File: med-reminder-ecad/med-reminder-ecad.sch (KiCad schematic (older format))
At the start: 38 parts, among them J1 USB_B_Micro, J2 22-03-5035, J3 22-03-5025, J4 22-03-5065, Q1 2N3904, Q2 2N3904, Q3 2N3904, Q4 2N3904, SW1 SW_SPDT, SW2 SW_Push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

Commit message: Changed OSC footprint size, changed switch footprint.
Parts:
- SW1: footprint Button_Switch_THT:SW_PUSH_6mm -> Button_Switch_THT:SW_Push_1P2T_Vertical_E-Switch_800UDP8P1A1M6
- Y1: footprint Oscillator:Oscillator_DIP-14 -> Oscillator:Oscillator_DIP-8; Mfg PN (none) -> MXO45HS-3C-8M0000
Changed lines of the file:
@@
 F 0 "SW1" H 1000 6835 50  0000 C CNN
 F 1 "SW_SPDT" H 1000 6744 50  0000 C CNN
-F 2 "Button_Switch_THT:SW_PUSH_6mm" H 1000 6550 50  0001 C CNN
+F 2 "Button_Switch_THT:SW_Push_1P2T_Vertical_E-Switch_800UDP8P1A1M6" H 1000 6550 50  0001 C CNN
 F 3 "~" H 1000 6550 50  0001 C CNN
 F 4 "1" H 1000 6550 50  0001 C CNN "DNP"
@@
 F 0 "Y1" H 6600 3268 50  0000 C CNN
 F 1 "8MHz" H 6600 3177 50  0000 C CNN
-F 2 "Oscillator:Oscillator_DIP-14" H 6600 3000 50  0001 C CNN
+F 2 "Oscillator:Oscillator_DIP-8" H 6600 3000 50  0001 C CNN
 F 3 "~" H 6600 3000 50  0001 C CNN
 F 4 "1" H 6600 3000 50  0001 C CNN "DNP"
+F 5 "MXO45HS-3C-8M0000" H 6600 3000 50  0001 C CNN "Mfg PN"
 	1    6600 3000
 	1    0    0    -1

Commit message: WIP update for PCB layout
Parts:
- C6: footprint Capacitor_THT:C_Rect_L7.0mm_W4.5mm_P5.00mm -> Capacitor_Tantalum_SMD:CP_EIA-3216-10_Kemet-I
- Y1: footprint Oscillator:Oscillator_DIP-8 -> Crystal:Crystal_HC33-U_Vertical
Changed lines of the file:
@@
 F 0 "C6" H 9092 1546 50  0000 L CNN
 F 1 "100nF" H 9092 1455 50  0000 L CNN
-F 2 "Capacitor_THT:C_Rect_L7.0mm_W4.5mm_P5.00mm" H 9000 1500 50  0001 C CNN
+F 2 "Capacitor_Tantalum_SMD:CP_EIA-3216-10_Kemet-I" H 9000 1500 50  0001 C CNN
 F 3 "~" H 9000 1500 50  0001 C CNN
 	1    9000 1500
@@
 F 0 "Y1" H 6600 3268 50  0000 C CNN
 F 1 "8MHz" H 6600 3177 50  0000 C CNN
-F 2 "Oscillator:Oscillator_DIP-8" H 6600 3000 50  0001 C CNN
+F 2 "Crystal:Crystal_HC33-U_Vertical" H 6600 3000 50  0001 C CNN
 F 3 "~" H 6600 3000 50  0001 C CNN
 F 4 "1" H 6600 3000 50  0001 C CNN "DNP"

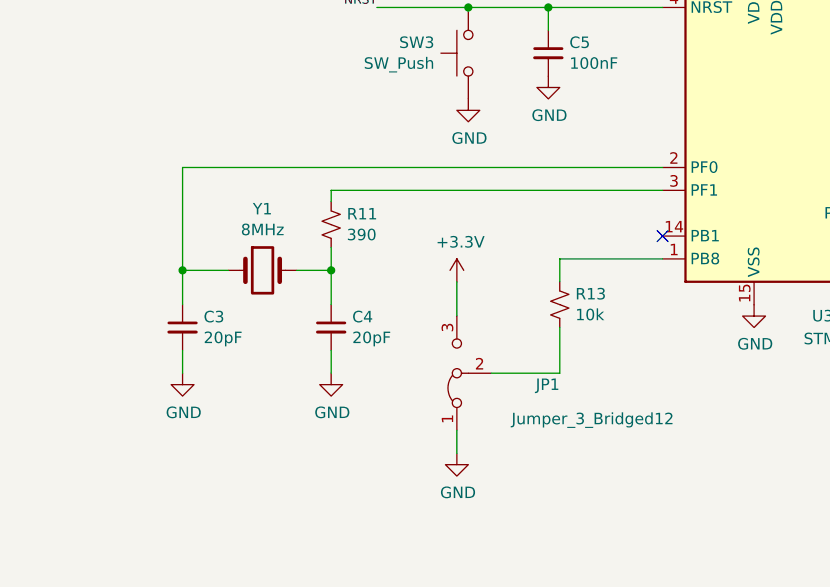
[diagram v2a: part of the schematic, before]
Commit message: Removed oscillator circuit
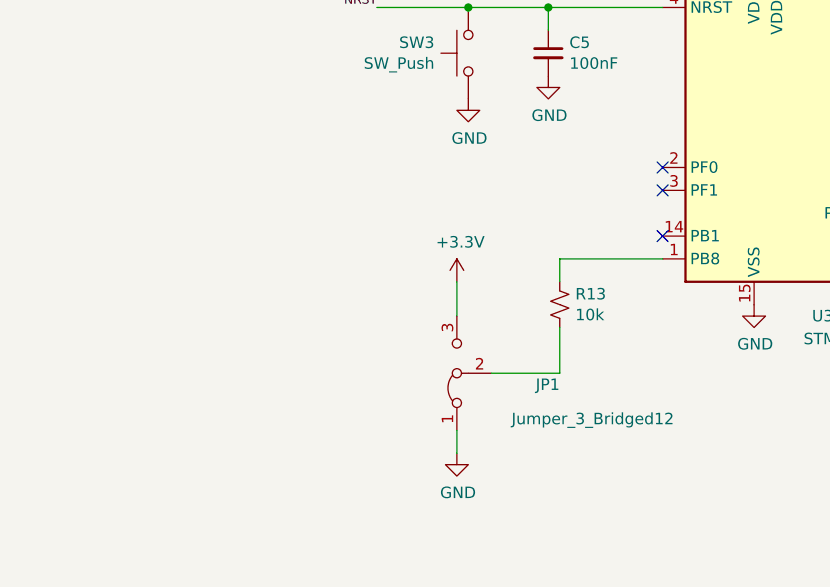
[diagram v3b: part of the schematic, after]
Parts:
- removed C3, C4: 20pF, Capacitor_THT:C_Rect_L7.0mm_W4.5mm_P5.00mm, symbol Device:C_Small
- removed R11: 390, Resistor_THT:R_Axial_DIN0204_L3.6mm_D1.6mm_P5.08mm_Horizontal, symbol Device:R_Small_US
- removed Y1: 8MHz, Crystal:Crystal_HC33-U_Vertical, symbol Device:Crystal
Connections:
- no-connect marks 5 -> 7
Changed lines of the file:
@@
 Connection ~ 9500 1600
-$Comp
-L Device:Crystal Y1
-U 1 1 60581513
-P 6600 3000
-F 0 "Y1" H 6600 3268 50  0000 C CNN
-F 1 "8MHz" H 6600 3177 50  0000 C CNN
-F 2 "Crystal:Crystal_HC33-U_Vertical" H 6600 3000 50  0001 C CNN
-F 3 "~" H 6600 3000 50  0001 C CNN
-F 4 "1" H 6600 3000 50  0001 C CNN "DNP"
-F 5 "MXO45HS-3C-8M0000" H 6600 3000 50  0001 C CNN "Mfg PN"
-	1    6600 3000
-	1    0    0    -1
-$EndComp
-$Comp
-L Device:C_Small C4
-U 1 1 60582666
-P 6900 3250
-F 0 "C4" H 6992 3296 50  0000 L CNN
-F 1 "20pF" H 6992 3205 50  0000 L CNN
-F 2 "Capacitor_THT:C_Rect_L7.0mm_W4.5mm_P5.00mm" H 6900 3250 50  0001 C CNN
-F 3 "~" H 6900 3250 50  0001 C CNN
-F 4 "1" H 6900 3250 50  0001 C CNN "DNP"
-	1    6900 3250
-	1    0    0    -1
-$EndComp
-$Comp
-L Device:C_Small C3
-U 1 1 60585144
-P 6250 3250
-F 0 "C3" H 6342 3296 50  0000 L CNN
-F 1 "20pF" H 6342 3205 50  0000 L CNN
-F 2 "Capacitor_THT:C_Rect_L7.0mm_W4.5mm_P5.00mm" H 6250 3250 50  0001 C CNN
-F 3 "~" H 6250 3250 50  0001 C CNN
-F 4 "1" H 6250 3250 50  0001 C CNN "DNP"
-	1    6250 3250
-	1    0    0    -1
-$EndComp
-$Comp
-L power:GND #PWR0110
-U 1 1 60585535
-P 6900 3450
-F 0 "#PWR0110" H 6900 3200 50  0001 C CNN
-F 1 "GND" H 6905 3277 50  0000 C CNN
-F 2 "" H 6900 3450 50  0001 C CNN
-F 3 "" H 6900 3450 50  0001 C CNN
-	1    6900 3450
-	1    0    0    -1
-$EndComp
-$Comp
-L power:GND #PWR0111
-U 1 1 60586789
-P 6250 3450
-F 0 "#PWR0111" H 6250 3200 50  0001 C CNN
-F 1 "GND" H 6255 3277 50  0000 C CNN
-F 2 "" H 6250 3450 50  0001 C CNN
-F 3 "" H 6250 3450 50  0001 C CNN
-	1    6250 3450
-	1    0    0    -1
-$EndComp
-Wire Wire Line
-	6250 3350 6250 3450
-Wire Wire Line
-	6900 3450 6900 3350
-Wire Wire Line
-	6900 3150 6900 3000
-Wire Wire Line
-	6900 3000 6750 3000
-Wire Wire Line
-	6250 3150 6250 3000
-Wire Wire Line
-	6250 3000 6450 3000
-Wire Wire Line
-	6250 2550 6250 3000
-Connection ~ 6250 3000
-$Comp
-L Device:R_Small_US R11
-U 1 1 6058A97D
-P 6900 2800
-F 0 "R11" H 6968 2846 50  0000 L CNN
-F 1 "390" H 6968 2755 50  0000 L CNN
-F 2 "Resistor_THT:R_Axial_DIN0204_L3.6mm_D1.6mm_P5.08mm_Horizontal" H 6900 2800 50  0001 C CNN
-F 3 "~" H 6900 2800 50  0001 C CNN
-F 4 "1" H 6900 2800 50  0001 C CNN "DNP"
-	1    6900 2800
-	1    0    0    -1
-$EndComp
-Wire Wire Line
-	6900 2900 6900 3000
-Connection ~ 6900 3000
-Wire Wire Line
-	6250 2550 8350 2550
-Wire Wire Line
-	6900 2700 6900 2650
-Wire Wire Line
-	6900 2650 8350 2650
 $Comp
 L Jumper:Jumper_3_Bridged12 JP1
@@
 Wire Wire Line
 	1600 2150 1600 2050
+NoConn ~ 8350 2550
+NoConn ~ 8350 2650
 $EndSCHEMATC

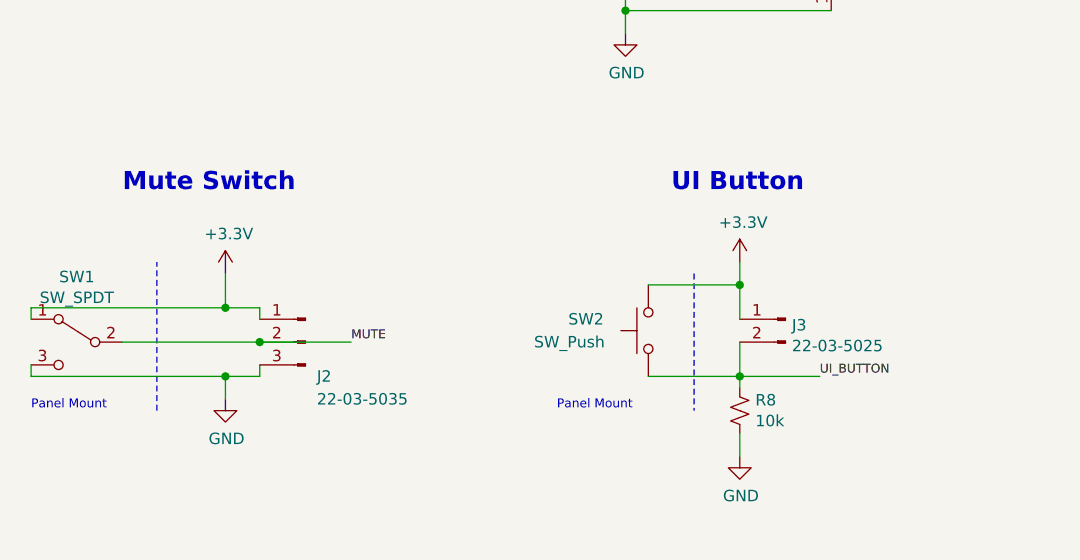
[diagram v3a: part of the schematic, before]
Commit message: Changed footprint of UI elements to be MOLEX SL connectors
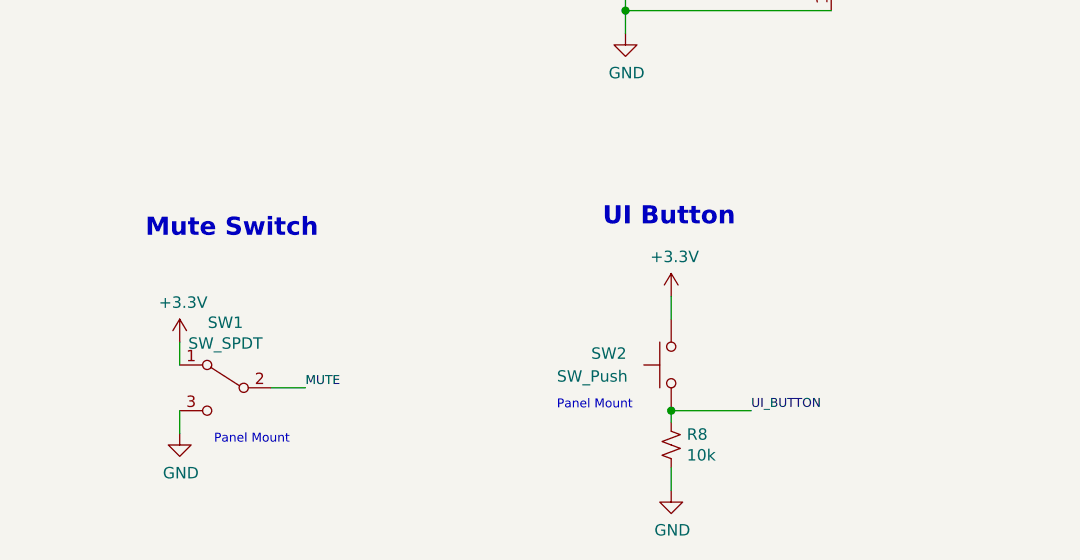
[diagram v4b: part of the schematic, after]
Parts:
- removed J2: 22-03-5035, Connector_Molex:Molex_SPOX_5267-03A_1x03_P2.50mm_Vertical, symbol Connector:Conn_01x03_Male
- removed J3: 22-03-5025, Connector_Molex:Molex_SPOX_5267-02A_1x02_P2.50mm_Vertical, symbol Connector:Conn_01x02_Male
- BZ1: footprint Connector_PinHeader_2.54mm:PinHeader_1x02_P2.54mm_Vertical -> Connector_Molex:Molex_SL_171971-0002_1x02_P2.54mm_Vertical
- SW1: footprint Button_Switch_THT:SW_Push_1P2T_Vertical_E-Switch_800UDP8P1A1M6 -> Connector_Molex:Molex_SL_171971-0003_1x03_P2.54mm_Vertical
- SW2: footprint Button_Switch_THT:SW_PUSH_6mm -> Connector_Molex:Molex_SL_171971-0002_1x02_P2.54mm_Vertical
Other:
- moved on the sheet: R8, SW1, SW2

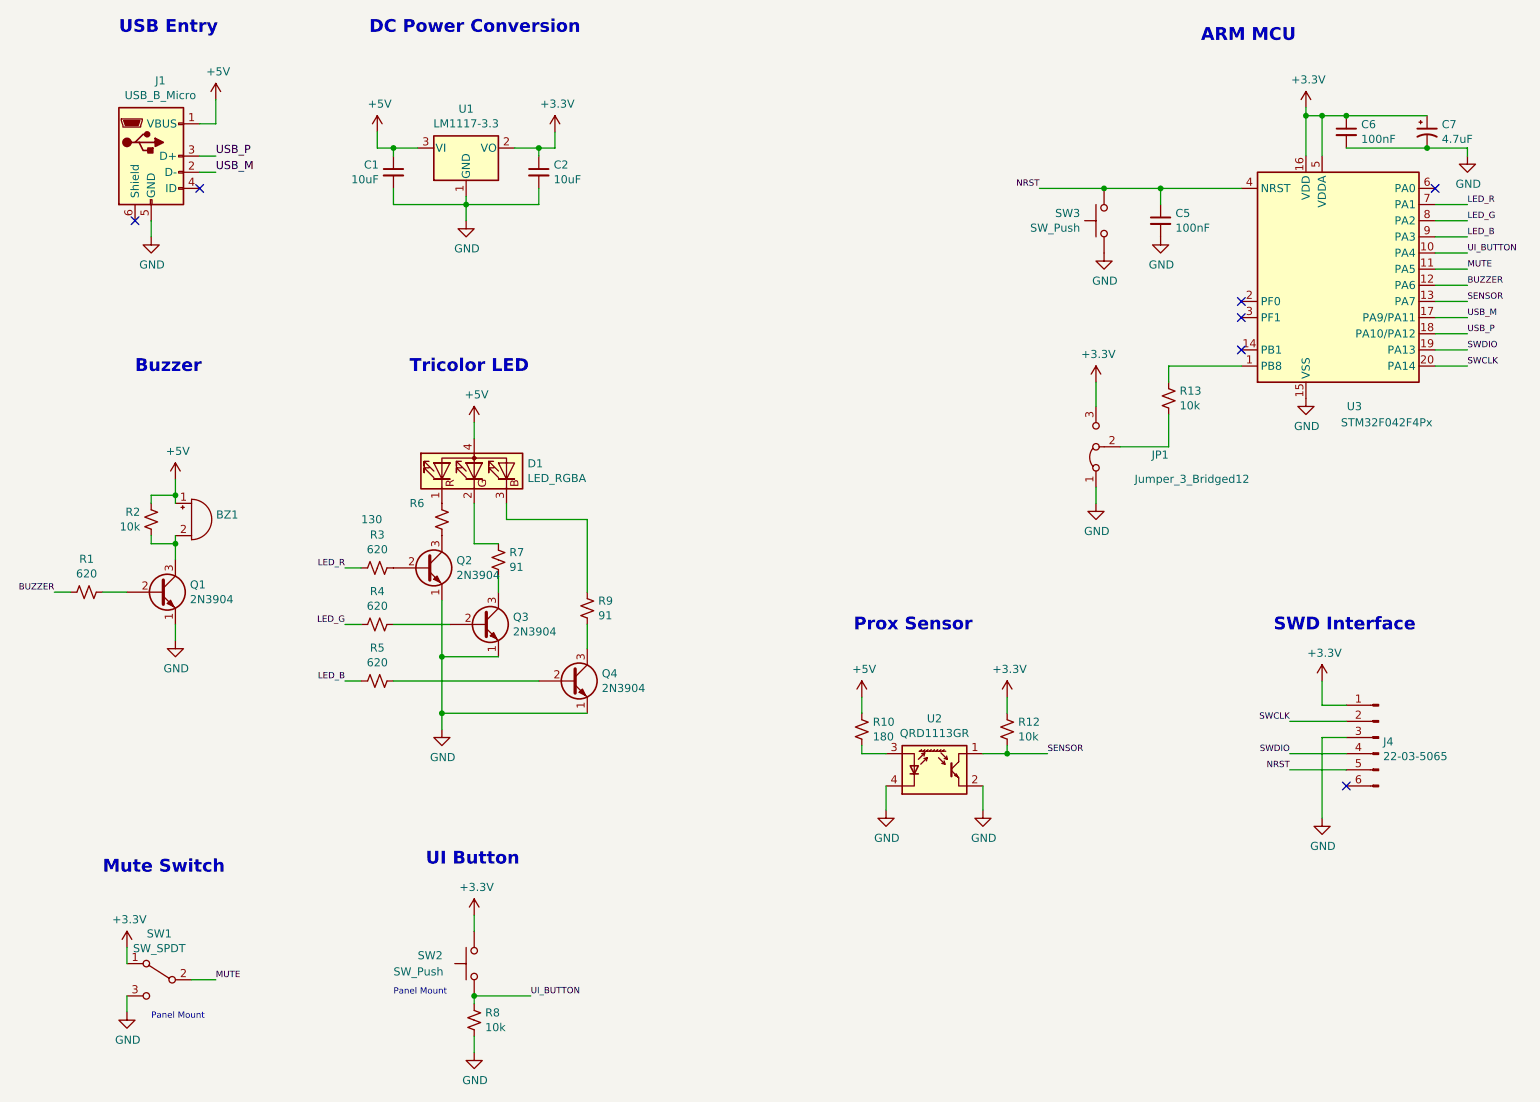
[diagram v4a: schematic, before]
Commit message: Broke out LED board to heirarchal sheet to become a separate board, replaced some components with SMD
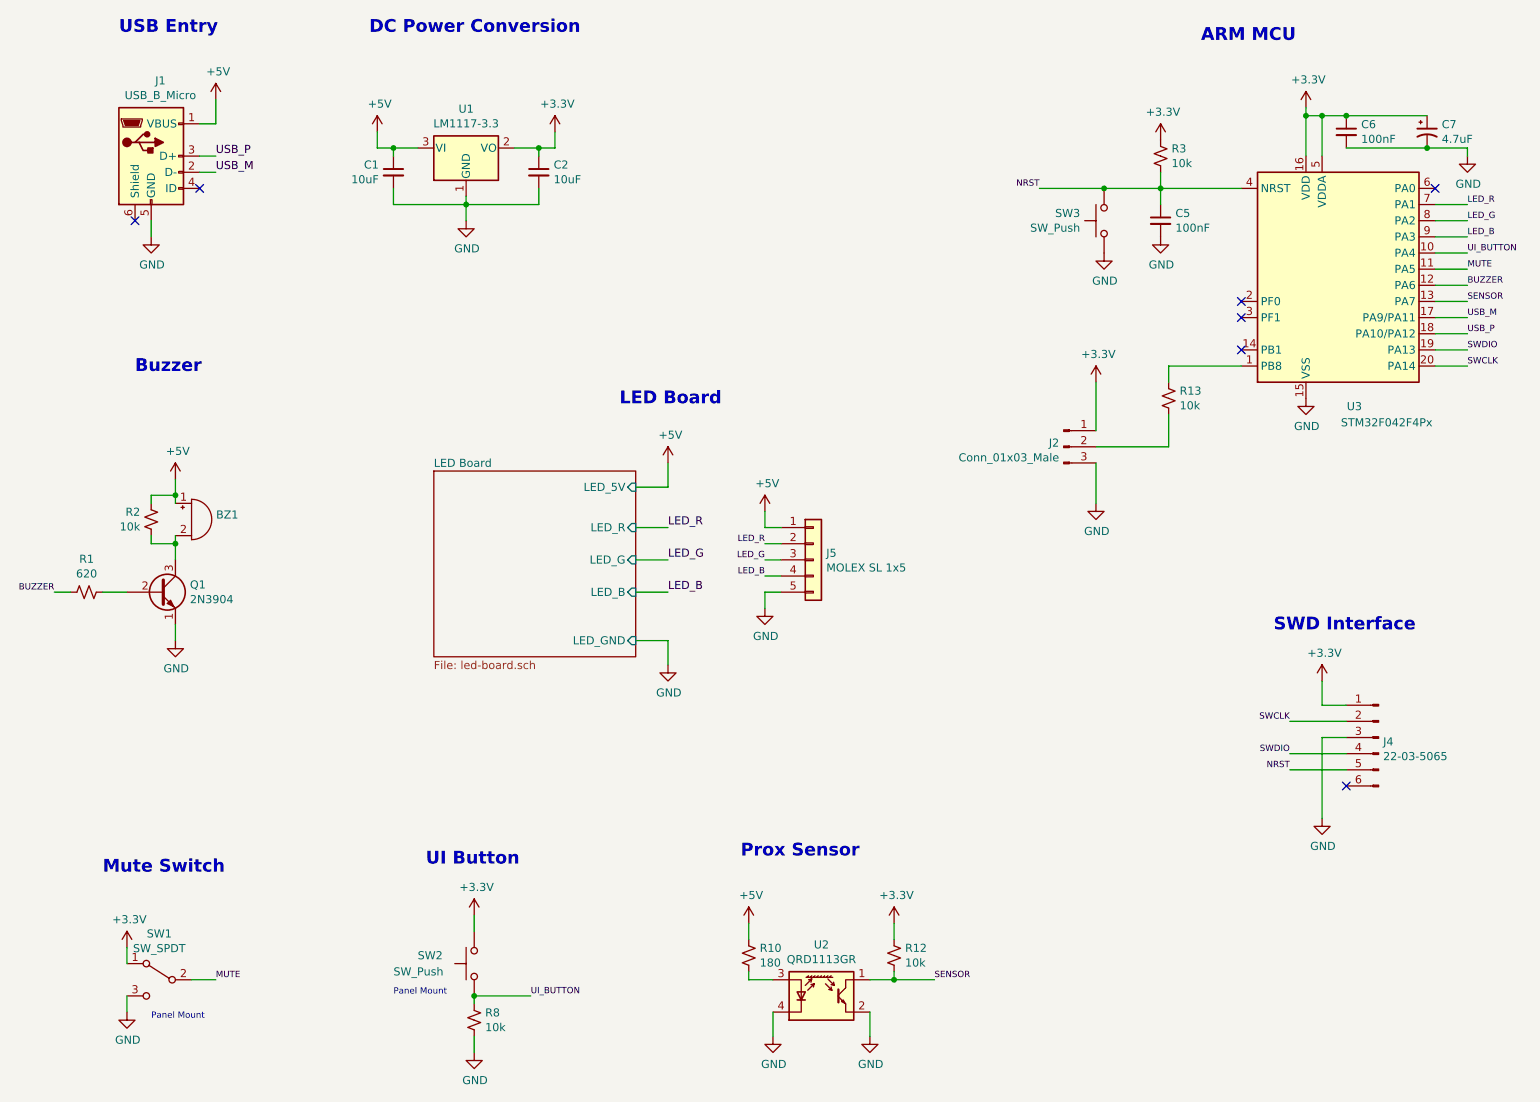
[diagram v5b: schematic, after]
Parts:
- removed D1: LED_RGBA, LED_THT:LED_D5.0mm-4_RGB, symbol Device:LED_RGBA
- removed JP1: Jumper_3_Bridged12, Connector_PinHeader_2.54mm:PinHeader_1x03_P2.54mm_Vertical, symbol Jumper:Jumper_3_Bridged12
- removed Q2, Q3, Q4: 2N3904, Package_TO_SOT_THT:TO-92_Inline, symbol Transistor_BJT:2N3904
- removed R4, R5: 620, Resistor_THT:R_Axial_DIN0204_L3.6mm_D1.6mm_P5.08mm_Horizontal, symbol Device:R_Small_US
- removed R6: 130, Resistor_THT:R_Axial_DIN0204_L3.6mm_D1.6mm_P5.08mm_Horizontal, symbol Device:R_Small_US
- removed R7, R9: 91, Resistor_THT:R_Axial_DIN0204_L3.6mm_D1.6mm_P5.08mm_Horizontal, symbol Device:R_Small_US
- added J2: Conn_01x03_Male, symbol Connector:Conn_01x03_Male
- added J5: MOLEX SL 1x5, Connector_Molex:Molex_SL_171971-0005_1x05_P2.54mm_Vertical, symbol Connector_Generic:Conn_01x05
- J1: footprint Connector_Molex:Molex_SPOX_5267-06A_1x06_P2.50mm_Vertical -> Connector_Molex:Molex_SL_171971-0006_1x06_P2.54mm_Vertical
- R3: value 620 -> 10k; Mfg Vishay -> (none); Mfg PN MBA02040C6200FC100 -> (none)
- SW3: footprint Button_Switch_THT:SW_PUSH_6mm -> jlcpcb:TACT_SWITCH_TS-1187A-X-X-X; DNP 1 -> (none); Mfg (none) -> XKB Connectivity; Mfg PN (none) -> TS-1187A-C-E-B
- U2: DNP (none) -> 1
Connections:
- net +3V3: now also R3.1, J2.1 (Pin_1)
- net +5V: now also J5.1 (Pin_1)
- net GND: now also J2.3 (Pin_3), J5.5 (Pin_5)
- net LED_B: now also J5.4 (Pin_4)
- net LED_G: now also J5.3 (Pin_3)
- net LED_R: now also J5.2 (Pin_2); no longer R3.1
- net NRST: now also R3.2
- net at R13.2: now also J2.2 (Pin_2)
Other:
- note added: "LED Board"
- note removed: "Tricolor LED"
- moved on the sheet: R10, R12, U2
